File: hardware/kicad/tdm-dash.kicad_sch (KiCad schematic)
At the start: 0 parts

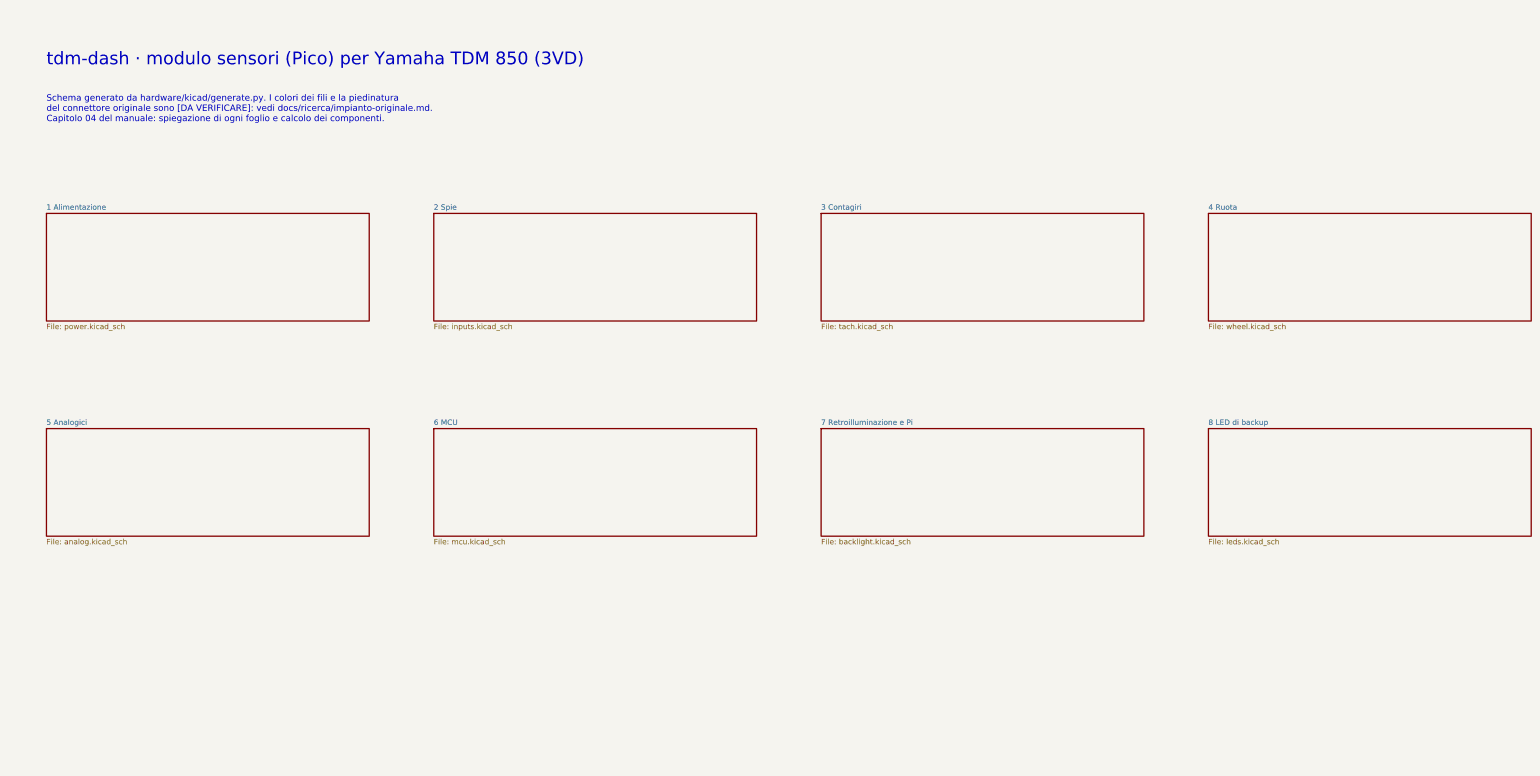
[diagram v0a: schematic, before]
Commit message: Translate code, hardware and docs to English; bilingual dashboard
- tdm-logic i18n module: every dashboard text in English and Italian,
  chosen by `[display] language` in the profile (English by default, the
  TDM 850 profile keeps Italian); number formatting per language
- Slint fixed labels moved to a `Labels` global filled from the same table;
  `tdm-dash --language en|it`; reference screens regenerated in English with
  Italian check screens
- tdmctl, tdm-dash CLI, simulator scenarios, calibration errors and tools
  print English
- KiCad sheets, WireViz harnesses, perfboard plan and CAD comments in
  English, exports regenerated with the new names
- manual, research, ADRs and READMEs translated; files renamed (docs/manual,
  docs/research, English chapter and ADR names); status markers are now
  [VERIFIED] / [TO VERIFY] / [HYPOTHESIS]

Co-Authored-By: Claude Opus 5.5 <noreply@anthropic.com>
Claude-Session: https://claude.ai/code/session_01G9D4Wshjz9MkaThp4wsrGP
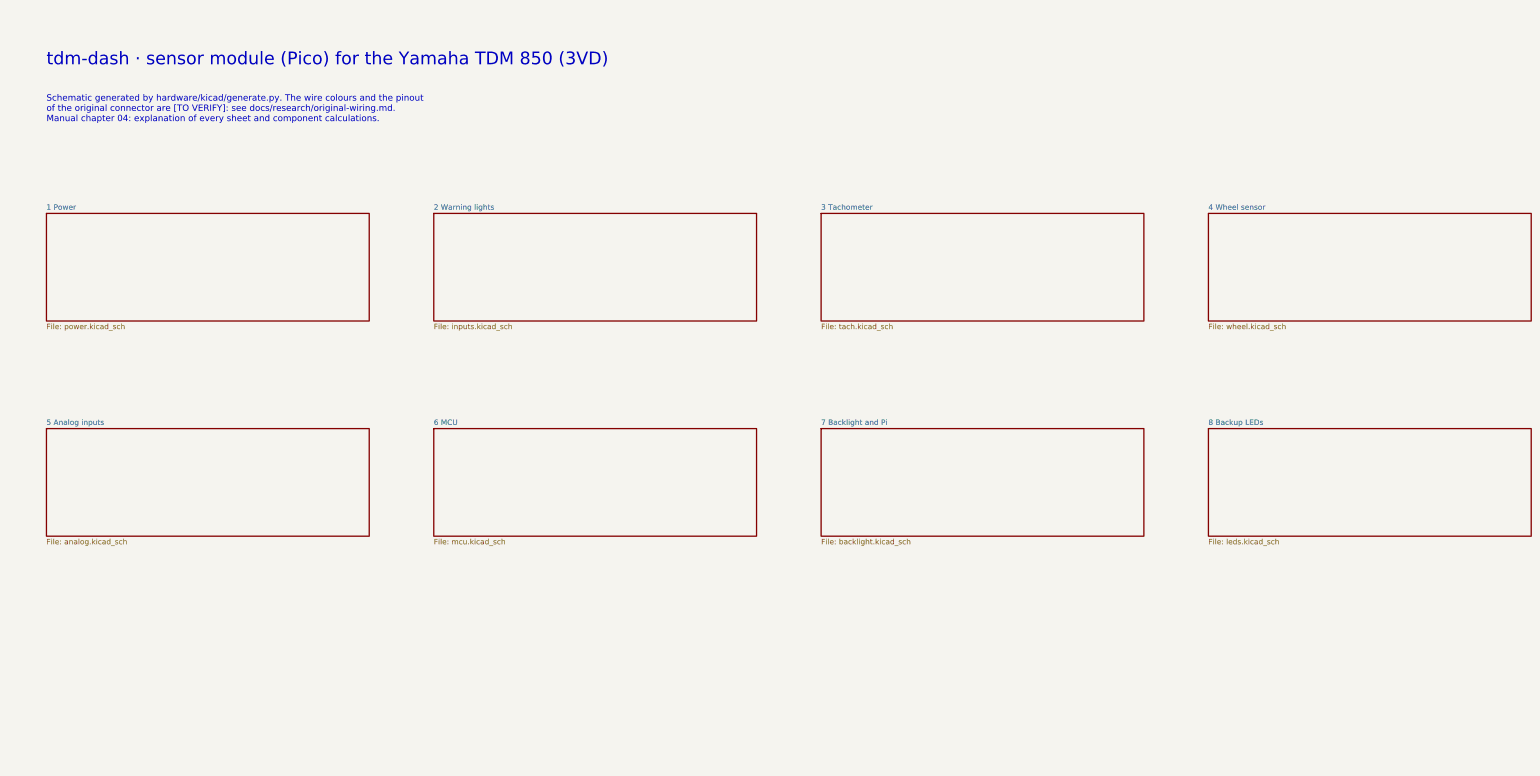
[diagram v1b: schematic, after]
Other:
- sheet 1 Alimentazione renamed 1 Power
- sheet 2 Spie renamed 2 Warning lights
- sheet 3 Contagiri renamed 3 Tachometer
- sheet 4 Ruota renamed 4 Wheel sensor
- sheet 5 Analogici renamed 5 Analog inputs
- sheet 7 Retroilluminazione e Pi renamed 7 Backlight and Pi
- sheet 8 LED di backup renamed 8 Backup LEDs
- note added: "Schematic generated by hardware/kicad/generate.py. The wire colours and the pinout of the original connector are [TO VERIFY]: see docs/research/original-wiring.md. Manual chapter 04: explanation of every sheet and component calculations."
- note added: "tdm-dash · sensor module (Pico) for the Yamaha TDM 850 (3VD)"
- note removed: "Schema generato da hardware/kicad/generate.py. I colori dei fili e la piedinatura del connettore originale sono [DA VERIFICARE]: vedi docs/ricerca/impianto-originale.md. Capitolo 04 del manuale: spiegazione di ogni foglio e calcolo dei componenti."
- note removed: "tdm-dash · modulo sensori (Pico) per Yamaha TDM 850 (3VD)"
- title: tdm-dash · modulo sensori -> tdm-dash · sensor module
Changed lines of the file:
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@@
 	(paper "A4")
 	(title_block
-		(title "tdm-dash · modulo sensori")
+		(title "tdm-dash · sensor module")
 		(date "2026-10-21")
 		(rev "0.1")
 		(company "tdm-dash · CERN-OHL-P-2.0")
-		(comment 1 "8 fogli")
-		(comment 2 "Generato da hardware/kicad/generate.py: non modificare a mano")
+		(comment 1 "8 sheets")
+		(comment 2 "Generated by hardware/kicad/generate.py: do not edit by hand")
 	)
 	(sheet
@@
 			(color 0 0 0 0)
 		)
-		(property "Sheetname" "1 Alimentazione"
+		(property "Sheetname" "1 Power"
 			(at 25.4 62.7884 0)
 			(effects
@@
 			(color 0 0 0 0)
 		)
-		(property "Sheetname" "2 Spie"
+		(property "Sheetname" "2 Warning lights"
 			(at 116.84 62.7884 0)
 			(effects
@@
 			(color 0 0 0 0)
 		)
-		(property "Sheetname" "3 Contagiri"
+		(property "Sheetname" "3 Tachometer"
 			(at 208.28 62.7884 0)
 			(effects
@@
 			(color 0 0 0 0)
 		)
-		(property "Sheetname" "4 Ruota"
+		(property "Sheetname" "4 Wheel sensor"
 			(at 299.72 62.7884 0)
 			(effects
@@
 			(color 0 0 0 0)
 		)
-		(property "Sheetname" "5 Analogici"
+		(property "Sheetname" "5 Analog inputs"
 			(at 25.4 113.5884 0)
 			(effects
@@
 			(color 0 0 0 0)
 		)
-		(property "Sheetname" "7 Retroilluminazione e Pi"
+		(property "Sheetname" "7 Backlight and Pi"
 			(at 208.28 113.5884 0)
 			(effects
@@
 			(color 0 0 0 0)
 		)
-		(property "Sheetname" "8 LED di backup"
+		(property "Sheetname" "8 Backup LEDs"
 			(at 299.72 113.5884 0)
 			(effects
@@
 		)
 	)
-	(text "tdm-dash · modulo sensori (Pico) per Yamaha TDM 850 (3VD)"
+	(text "tdm-dash · sensor module (Pico) for the Yamaha TDM 850 (3VD)"
 		(exclude_from_sim no)
 		(at 25.4 25.4 0)
@@
 		)
 	)
-	(text "Schema generato da hardware/kicad/generate.py. I colori dei fili e la piedinatura\ndel connettore originale sono [DA VERIFICARE]: vedi docs/ricerca/impianto-originale.md.\nCapitolo 04 del manuale: spiegazione di ogni foglio e calcolo dei componenti."
+	(text "Schematic generated by hardware/kicad/generate.py. The wire colours and the pinout\nof the original connector are [TO VERIFY]: see docs/research/original-wiring.md.\nManual chapter 04: explanation of every sheet and component calculations."
 		(exclude_from_sim no)
 		(at 25.4 35.56 0)

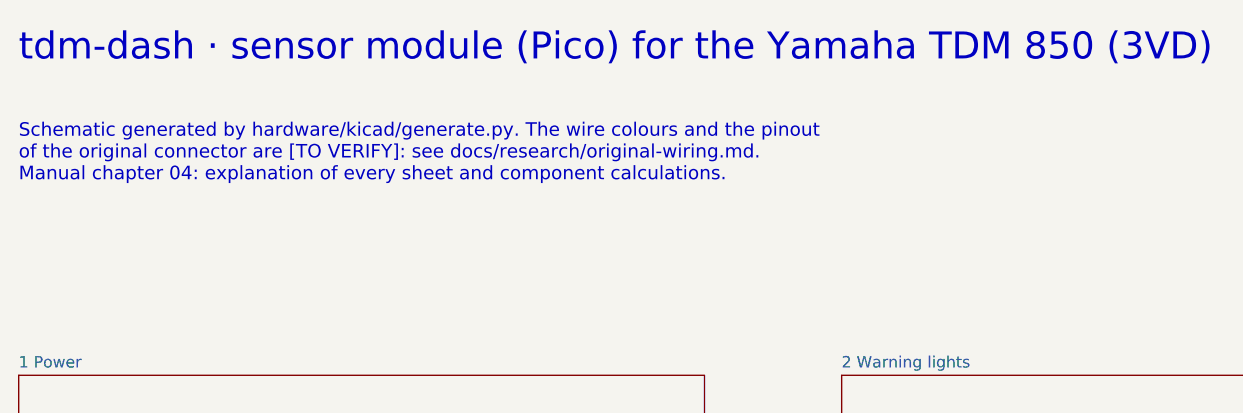
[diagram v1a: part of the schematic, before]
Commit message: English README, ADR 0012, CLAUDE.md rules, banner; consistent spelling
- README and docs/assets in English, banner tagline "Open-source digital
  instrument cluster" and regenerated banner
- ADR 0012: English repository, bilingual dashboard
- CLAUDE.md: English everywhere, dashboard texts in both languages through
  tdm-logic i18n, new status markers
- American spelling across docs, harness labels and schematic notes;
  ADR 0007 renamed to 0007-licenses; exports and screens regenerated

Co-Authored-By: Claude Opus 5.5 <noreply@anthropic.com>
Claude-Session: https://claude.ai/code/session_01G9D4Wshjz9MkaThp4wsrGP
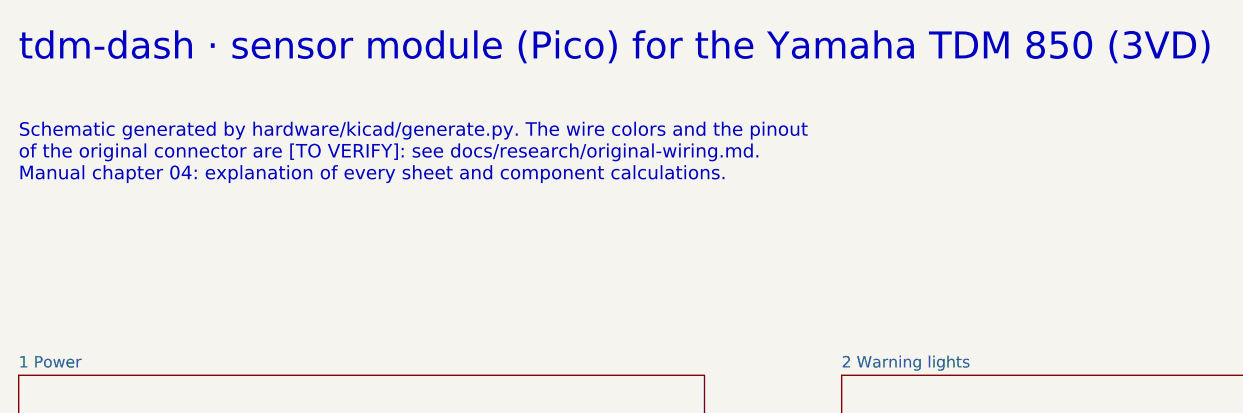
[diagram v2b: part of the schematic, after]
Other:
- note added: "Schematic generated by hardware/kicad/generate.py. The wire colors and the pinout of the original connector are [TO VERIFY]: see docs/research/original-wiring.md. Manual chapter 04: explanation of every sheet and component calculations."
- note removed: "Schematic generated by hardware/kicad/generate.py. The wire colours and the pinout of the original connector are [TO VERIFY]: see docs/research/original-wiring.md. Manual chapter 04: explanation of every sheet and component calculations."
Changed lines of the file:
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@@
 		)
 	)
-	(text "Schematic generated by hardware/kicad/generate.py. The wire colours and the pinout\nof the original connector are [TO VERIFY]: see docs/research/original-wiring.md.\nManual chapter 04: explanation of every sheet and component calculations."
+	(text "Schematic generated by hardware/kicad/generate.py. The wire colors and the pinout\nof the original connector are [TO VERIFY]: see docs/research/original-wiring.md.\nManual chapter 04: explanation of every sheet and component calculations."
 		(exclude_from_sim no)
 		(at 25.4 35.56 0)

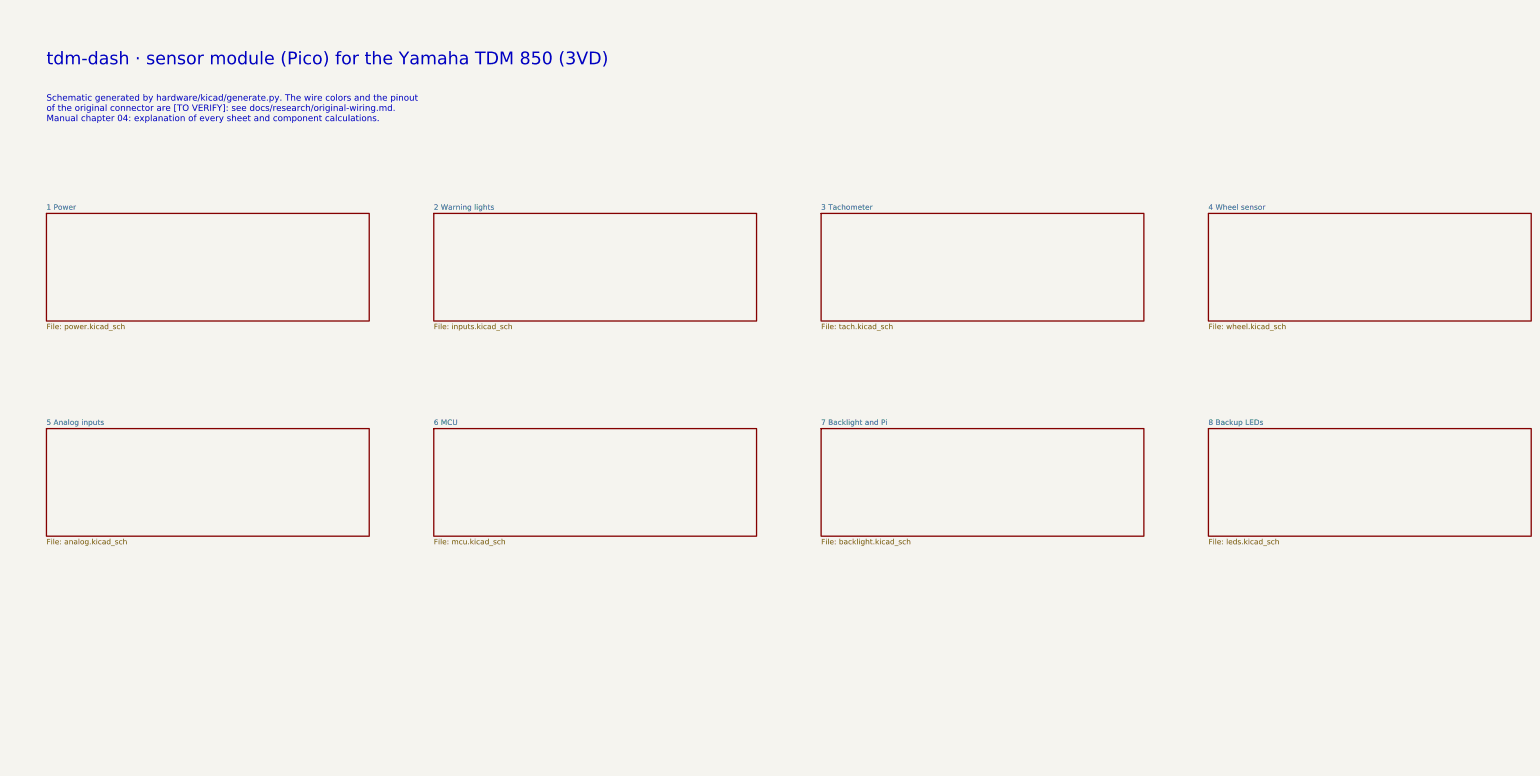
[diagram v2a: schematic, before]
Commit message: Schematic: drawn wires, block diagram, new title block
The sheets were a netlist in disguise: every pin ended in a short stub and
a label, so the circuits had to be pieced together by name, labels
overlapped, two sheets fell off the index page and the title block was
KiCad's default. The generator now draws the schematic:

- hardware/kicad/schgen: placement on the 50 mil grid, orthogonal wires,
  junctions, hierarchical ports, module and connector symbols with named
  pins; the drawing is normalised the way KiCad 9 reads it and checked
  against the declared netlist (no wire may connect anything else)
- hardware/kicad/sheets: one module per sheet, laid out left to right
  from the bike to the Pico; the root sheet is a block diagram whose
  wires are the signals between sheets
- tdm-dash.kicad_wks: frame and title block of the project
- symbols copied from KiCad 9.0.9 (vendor_symbols.py): the generator no
  longer needs KiCad installed
- export.sh: ERC, tools/check_netlist.py (KiCad's netlist is the declared
  one), check_pinmap.py, PDF and SVG on white, tools/check_svg_layout.py
  (no text over another text, a wire, the frame or the title block)

The circuit is unchanged: KiCad's netlist of the old and new schematic
has the same 56 nets (FRAM pins now follow the breakout header, R603/R604
pins swapped).

Co-Authored-By: Claude Opus 5.5 <noreply@anthropic.com>
Claude-Session: https://claude.ai/code/session_01G9D4Wshjz9MkaThp4wsrGP
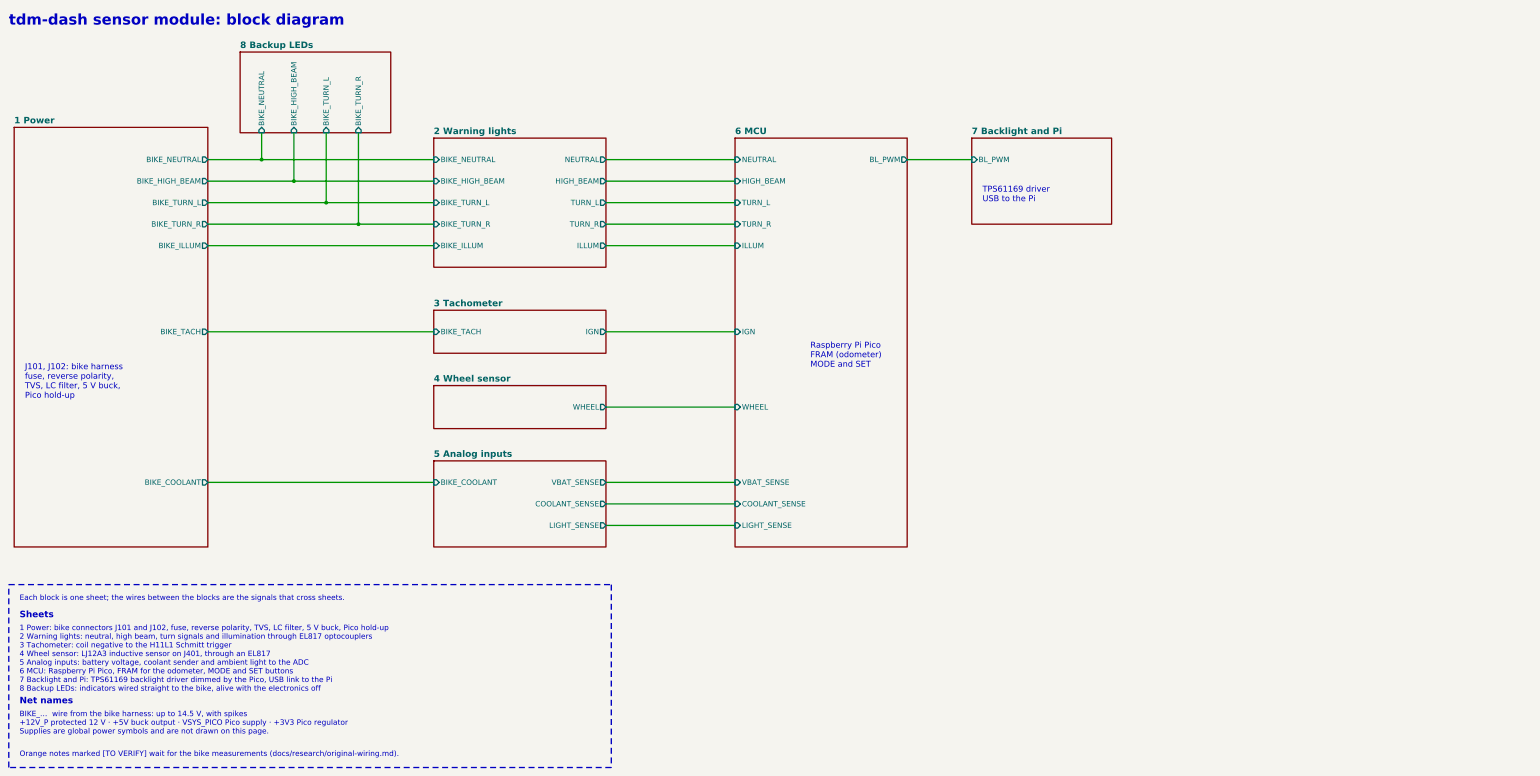
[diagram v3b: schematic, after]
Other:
- sheet 1 Power ports: added BIKE_COOLANT, BIKE_HIGH_BEAM, BIKE_ILLUM, BIKE_NEUTRAL, BIKE_TACH, BIKE_TURN_L, BIKE_TURN_R; removed none
- sheet 2 Warning lights ports: added BIKE_HIGH_BEAM, BIKE_ILLUM, BIKE_NEUTRAL, BIKE_TURN_L, BIKE_TURN_R, HIGH_BEAM, ILLUM, NEUTRAL, TURN_L, TURN_R; removed none
- sheet 3 Tachometer ports: added BIKE_TACH, IGN; removed none
- sheet 4 Wheel sensor ports: added WHEEL; removed none
- sheet 5 Analog inputs ports: added BIKE_COOLANT, COOLANT_SENSE, LIGHT_SENSE, VBAT_SENSE; removed none
- sheet 6 MCU ports: added BL_PWM, COOLANT_SENSE, HIGH_BEAM, IGN, ILLUM, LIGHT_SENSE, NEUTRAL, TURN_L, TURN_R, VBAT_SENSE, WHEEL; removed none
- sheet 7 Backlight and Pi ports: added BL_PWM; removed none
- sheet 8 Backup LEDs ports: added BIKE_HIGH_BEAM, BIKE_NEUTRAL, BIKE_TURN_L, BIKE_TURN_R; removed none
- note added: "1 Power: bike connectors J101 and J102, fuse, reverse polarity, TVS, LC filter, 5 V buck, Pico hold-up 2 Warning lights: neutral, high beam, turn signals and illumination through EL817 optocouplers 3 Tachometer: coil negative to the H11L1 Schmitt trigger 4 Wheel sensor: LJ12A3 inductive sensor on J401, through an EL817 5 Analog inputs: battery voltage, coolant sender and ambient light to the ADC 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"
- note added: "BIKE_… wire from the bike harness: up to 14.5 V, with spikes +12V_P protected 12 V · +5V buck output · VSYS_PICO Pico supply · +3V3 Pico regulator Supplies are global power symbols and are not drawn on this page."
- note added: "Each block is one sheet; the wires between the blocks are the signals that cross sheets."
- note added: "J101, J102: bike harness fuse, reverse polarity, TVS, LC filter, 5 V buck, Pico hold-up"
- note added: "Net names"
- note added: "Orange notes marked [TO VERIFY] wait for the bike measurements (docs/research/original-wiring.md)."
- note added: "Raspberry Pi Pico FRAM (odometer) MODE and SET"
- note added: "Sheets"
- note added: "TPS61169 driver USB to the Pi"
- note added: "tdm-dash sensor module: block diagram"
- note removed: "Schematic generated by hardware/kicad/generate.py. The wire colors and the pinout of the original connector are [TO VERIFY]: see docs/research/original-wiring.md. Manual chapter 04: explanation of every sheet and component calculations."
- note removed: "tdm-dash · sensor module (Pico) for the Yamaha TDM 850 (3VD)"
- company: tdm-dash · CERN-OHL-P-2.0 -> tdm-dash
- title: tdm-dash · sensor module -> Overview: block diagram
